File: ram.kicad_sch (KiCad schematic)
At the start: 59 parts, among them U2 MT41K512M8DA, U5 AS6C8008-55ZIN

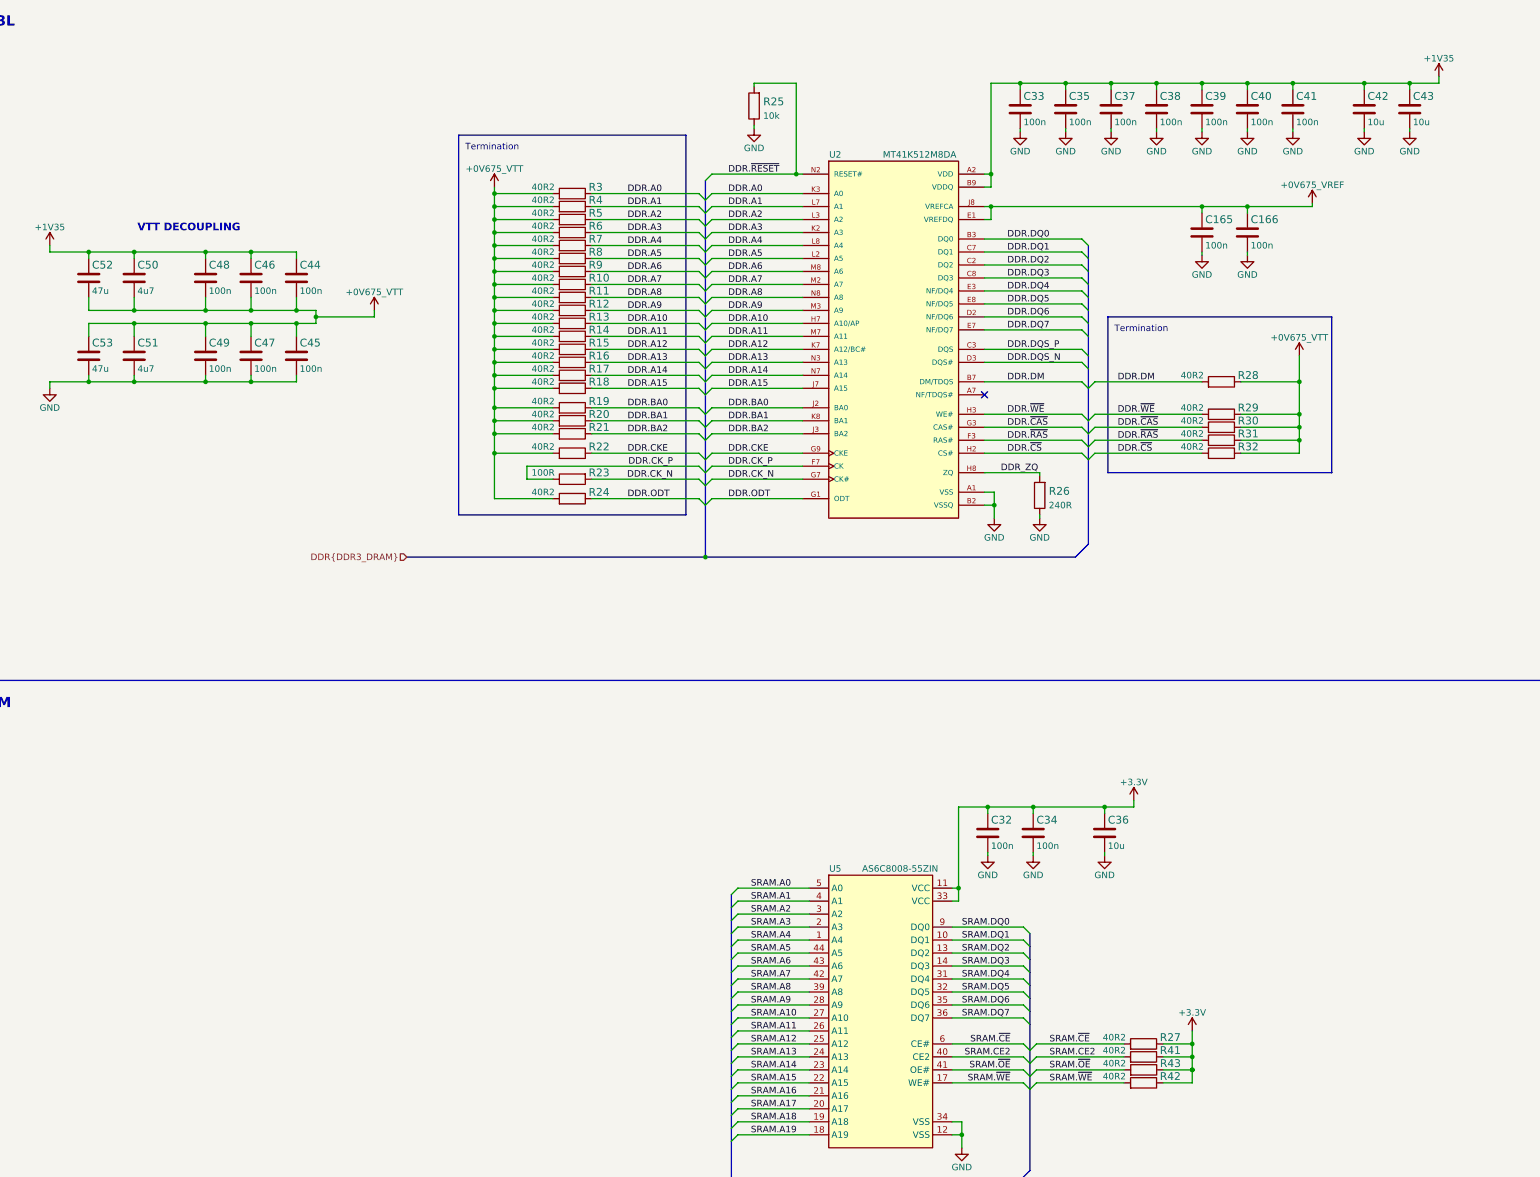
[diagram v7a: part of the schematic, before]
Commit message: Re-annotate the schematic. Export changes to PCB
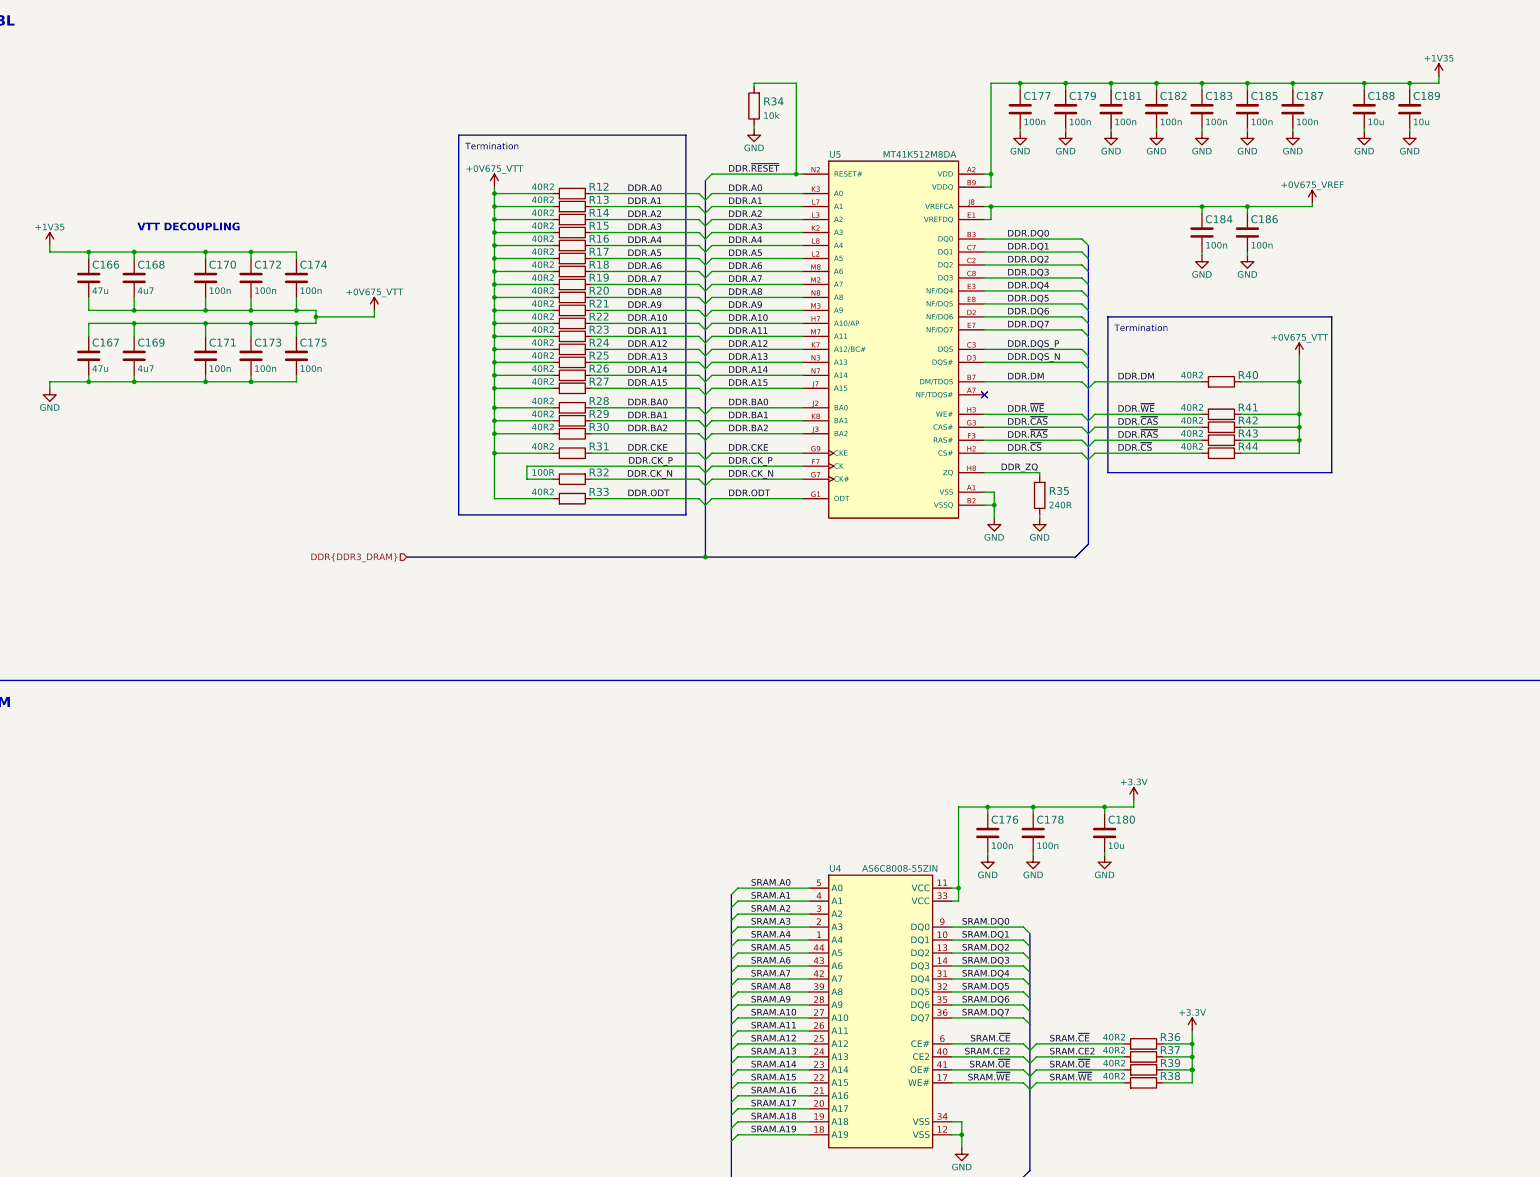
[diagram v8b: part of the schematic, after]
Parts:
- renumbered C52 to C166, C53 to C167, C50 to C168, C51 to C169, C48 to C170, C49 to C171, C46 to C172, C47 to C173, C44 to C174, C45 to C175, C32 to C176, C33 to C177, C34 to C178, C35 to C179, C36 to C180, C37 to C181, C38 to C182, C39 to C183, C165 to C184, C40 to C185, C166 to C186, C41 to C187, C42 to C188, C43 to C189, R3 to R12, R4 to R13, R5 to R14, R6 to R15, R7 to R16, R8 to R17, R9 to R18, R10 to R19, R11 to R20, R12 to R21, R13 to R22, R14 to R23, R15 to R24, R16 to R25, R17 to R26, R18 to R27, R19 to R28, R20 to R29, R21 to R30, R22 to R31, R23 to R32, R24 to R33, R25 to R34, R26 to R35, R27 to R36, R41 to R37, R42 to R38, R43 to R39, R28 to R40, R29 to R41, R30 to R42, R31 to R43, R32 to R44, U5 to U4, U2 to U5
